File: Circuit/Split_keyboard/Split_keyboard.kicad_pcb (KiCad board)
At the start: 2 copper layers, 62 parts, among them SW27 SW_Push, SW28 SW_Push, SW29 SW_Push, SW30 SW_Push, SW31 SW_Push, SW32 SW_Push, SW33 SW_Push, SW34 SW_Push, SW35 SW_Push, SW36 SW_Push, SW37 SW_Push, SW38 SW_Push, SW39 SW_Push, SW40 SW_Push, SW41 SW_Push, SW42 SW_Push, SW43 SW_Push, SW44 SW_Push, SW45 SW_Push, SW46 SW_Push, SW47 SW_Push, SW48 SW_Push, SW49 SW_Push, SW50 SW_Push, SW51 SW_Push, SW52 SW_Push, U2 XIAO-nRF52840-SMD

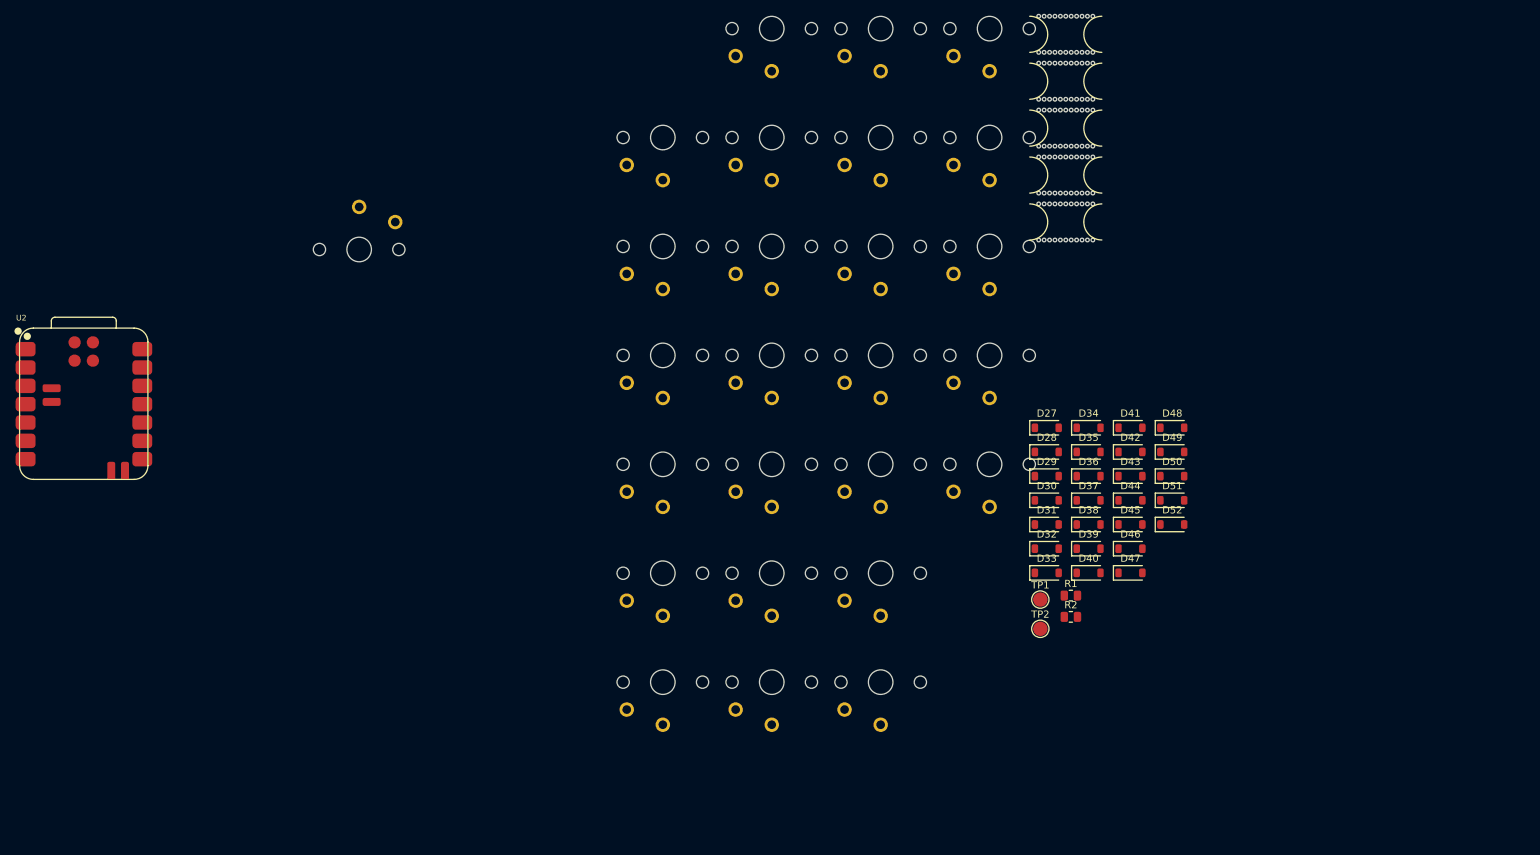
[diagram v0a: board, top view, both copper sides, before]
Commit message: Changed the design of the footprints and maded it simliar to keeb.io keyboards
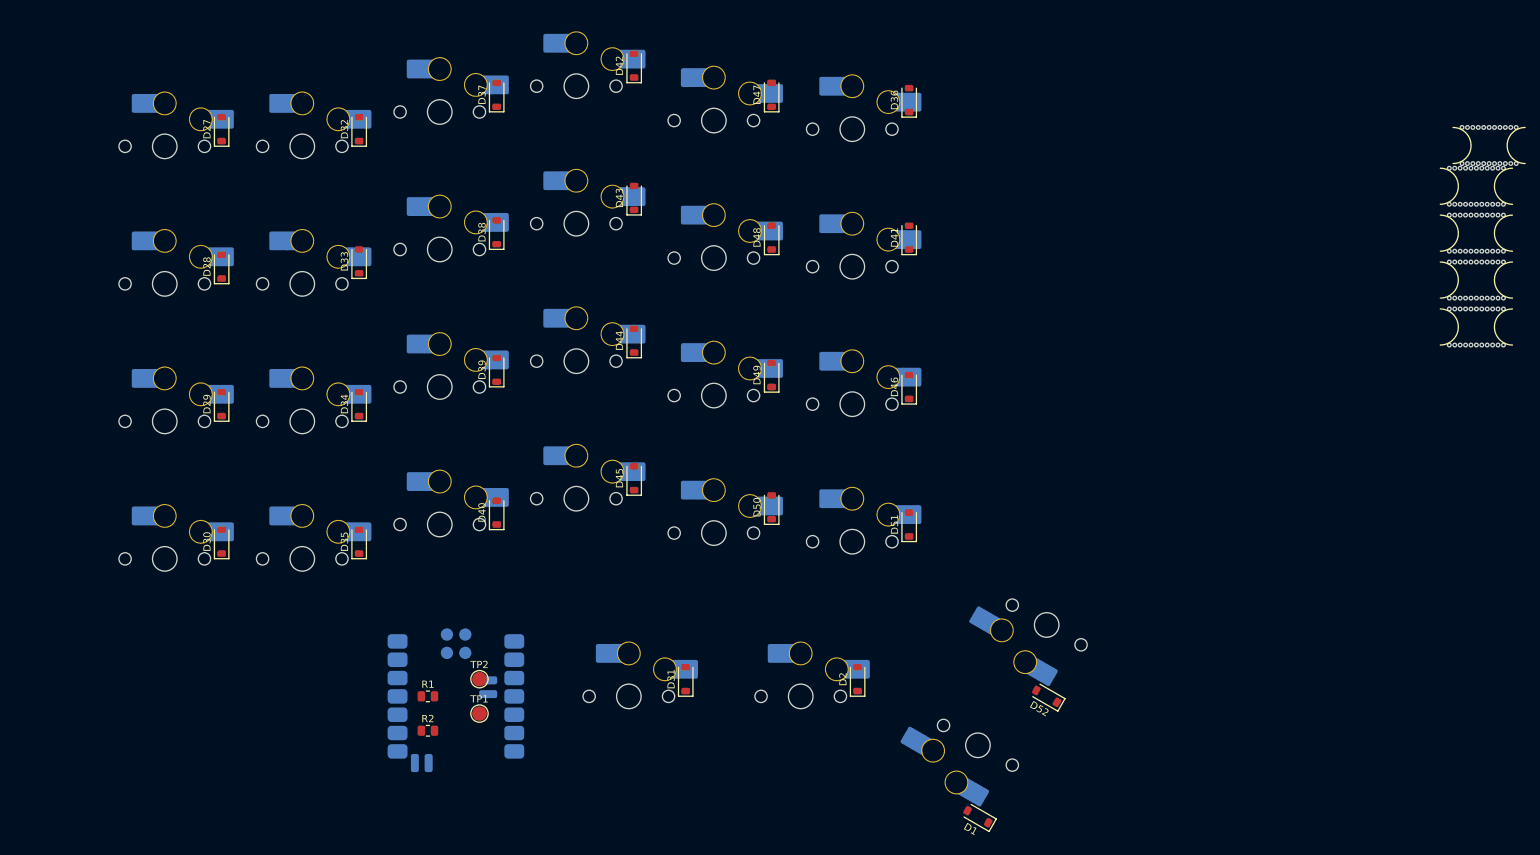
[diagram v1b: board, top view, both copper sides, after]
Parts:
- added D1: D, Diode_SMD:D_SOD-123, F.Cu at (169.1, 157.2)
- added D2: D, Diode_SMD:D_SOD-123, F.Cu at (152.4, 138.1)
- added SW1: SW_Push, marbastlib-choc:SW_choc_v1_HS_CPG135001S30_1u, B.Cu at (169.1, 147.3)
- added SW2: SW_Push, marbastlib-choc:SW_choc_v1_HS_CPG135001S30_1u, B.Cu at (144.5, 140.5)
- SW27, SW28, SW29, SW30, SW31, SW32, SW33, SW34, SW35, SW36, SW37, SW38, SW39, SW40, SW41, SW42, SW43, SW44, SW45, SW46, SW47, SW48, SW49, SW50, SW51, SW52: footprint marbastlib-choc:SW_choc_v1_1u -> marbastlib-choc:SW_choc_v1_HS_CPG135001S30_1u; moved to B.Cu
- U2: moved to B.Cu
- moved D27 121.6 mm to (64.3, 61.9), turned to 90 degrees
- moved D28 117.2 mm to (64.3, 81.0), turned to 90 degrees
- moved D29 114.7 mm to (64.3, 100.0), turned to 90 degrees
- moved D30 114.5 mm to (64.3, 119.1), turned to 90 degrees
- moved D32 111.6 mm to (83.3, 61.9), turned to 90 degrees
- moved D33 104.6 mm to (83.3, 80.2), turned to 90 degrees
- moved D35 101.8 mm to (83.3, 119.1), turned to 90 degrees
- moved D34 101.1 mm to (83.3, 100.0), turned to 90 degrees
- moved D37 99.4 mm to (102.4, 57.1), turned to 90 degrees
- moved D38 91.5 mm to (102.4, 76.2), turned to 90 degrees
- moved R2 90.5 mm to (92.9, 145.3)
- moved R1 90.2 mm to (92.9, 140.5)
- moved SW35 87.4 mm to (75.5, 121.4)
- moved D42 87.1 mm to (121.4, 53.1), turned to 90 degrees
- moved D39 85.7 mm to (102.4, 95.2), turned to 90 degrees
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
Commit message: Added right side and added edge.cuts for the pcb on both sides
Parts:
- added BO10: Break Off, Panelization.pretty-master:mouse-bite-5mm-slot, F.Cu at (175.5, 67.5)
- added BO6: Break Off, Panelization.pretty-master:mouse-bite-5mm-slot, F.Cu at (172.9, 38.6)
- added BO7: Break Off, Panelization.pretty-master:mouse-bite-5mm-slot, F.Cu at (172.9, 45.1)
- added BO8: Break off, Panelization.pretty-master:mouse-bite-5mm-slot, F.Cu at (172.9, 51.6)
- added BO9: Break Off, Panelization.pretty-master:mouse-bite-5mm-slot, F.Cu at (172.9, 58.1)
- added D10: D, Diode_SMD:D_SOD-123, B.Cu at (192.9, 81.0)
- added D11: D, Diode_SMD:D_SOD-123, B.Cu at (288.1, 61.9)
- added D12: D, Diode_SMD:D_SOD-123, B.Cu at (269.1, 81.0)
- added D13: D, Diode_SMD:D_SOD-123, B.Cu at (250.0, 115.0)
- added D14: D, Diode_SMD:D_SOD-123, B.Cu at (250.0, 60.3)
- added D15: D, Diode_SMD:D_SOD-123, B.Cu at (231.0, 57.1)
- added D16: D, Diode_SMD:D_SOD-123, B.Cu at (231.0, 76.2)
- added D17: D, Diode_SMD:D_SOD-123, B.Cu at (192.9, 61.9)
- added D18: D, Diode_SMD:D_SOD-123, B.Cu at (288.1, 81.0)
- added D19: D, Diode_SMD:D_SOD-123, B.Cu at (269.1, 98.4)
- added D20: D, Diode_SMD:D_SOD-123, B.Cu at (269.1, 61.9)
- added D21: D, Diode_SMD:D_SOD-123, B.Cu at (250.0, 96.0)
- added D22: D, Diode_SMD:D_SOD-123, B.Cu at (250.0, 78.6)
- added D23: D, Diode_SMD:D_SOD-123, B.Cu at (192.9, 98.4)
- added D24: D, Diode_SMD:D_SOD-123, B.Cu at (288.1, 119.1)
- added D25: D, Diode_SMD:D_SOD-123, B.Cu at (288.1, 98.4)
- added D26: D, Diode_SMD:D_SOD-123, B.Cu at (269.1, 117.4)
- added D3: D, Diode_SMD:D_SOD-123, B.Cu at (192.9, 119.1)
- added D4: D, Diode_SMD:D_SOD-123, B.Cu at (211.9, 115.0)
- added D5: D, Diode_SMD:D_SOD-123, B.Cu at (211.9, 96.0)
- added D53: D, Diode_SMD:D_SOD-123, B.Cu at (226.2, 140.5)
- added D54: D, Diode_SMD:D_SOD-123, B.Cu at (192.9, 150.0)
- added D55: D, Diode_SMD:D_SOD-123, B.Cu at (202.4, 140.5)
- added D56: D, Diode_SMD:D_SOD-123, B.Cu at (181.0, 135.7)
- added D6: D, Diode_SMD:D_SOD-123, B.Cu at (231.0, 114.3)
- added D7: D, Diode_SMD:D_SOD-123, B.Cu at (231.0, 95.2)
- added D8: D, Diode_SMD:D_SOD-123, B.Cu at (211.9, 59.5)
- added D9: D, Diode_SMD:D_SOD-123, B.Cu at (211.9, 78.6)
- added R3: 806k, Resistor_SMD:R_0805_2012Metric, F.Cu at (278.7, 27.9)
- added R4: 2M, Resistor_SMD:R_0805_2012Metric, F.Cu at (278.7, 30.8)
- added SW10: SW_Push, marbastlib-choc:SW_choc_v1_HS_CPG135001S30_1u, B.Cu at (200.8, 81.0)
- added SW11: SW_Push, marbastlib-choc:SW_choc_v1_HS_CPG135001S30_1u, B.Cu at (296.0, 61.9)
- added SW12: SW_Push, marbastlib-choc:SW_choc_v1_HS_CPG135001S30_1u, B.Cu at (277.0, 81.0)
- added SW13: SW_Push, marbastlib-choc:SW_choc_v1_HS_CPG135001S30_1u, B.Cu at (257.9, 116.7)
- added SW14: SW_Push, marbastlib-choc:SW_choc_v1_HS_CPG135001S30_1u, B.Cu at (257.9, 59.5)
- added SW15: SW_Push, marbastlib-choc:SW_choc_v1_HS_CPG135001S30_1u, B.Cu at (238.9, 57.1)
- added SW16: SW_Push, marbastlib-choc:SW_choc_v1_HS_CPG135001S30_1u, B.Cu at (238.9, 76.2)
- added SW17: SW_Push, marbastlib-choc:SW_choc_v1_HS_CPG135001S30_1u, B.Cu at (200.8, 61.9)
- added SW18: SW_Push, marbastlib-choc:SW_choc_v1_HS_CPG135001S30_1u, B.Cu at (296.0, 81.0)
- added SW19: SW_Push, marbastlib-choc:SW_choc_v1_HS_CPG135001S30_1u, B.Cu at (277.0, 100.0)
- added SW20: SW_Push, marbastlib-choc:SW_choc_v1_HS_CPG135001S30_1u, B.Cu at (277.0, 61.9)
- added SW21: SW_Push, marbastlib-choc:SW_choc_v1_HS_CPG135001S30_1u, B.Cu at (257.9, 97.6)
- added SW22: SW_Push, marbastlib-choc:SW_choc_v1_HS_CPG135001S30_1u, B.Cu at (257.9, 78.6)
- added SW23: SW_Push, marbastlib-choc:SW_choc_v1_HS_CPG135001S30_1u, B.Cu at (200.8, 100.0)
- added SW24: SW_Push, marbastlib-choc:SW_choc_v1_HS_CPG135001S30_1u, B.Cu at (296.0, 119.1)
- added SW25: SW_Push, marbastlib-choc:SW_choc_v1_HS_CPG135001S30_1u, B.Cu at (296.0, 100.0)
- added SW26: SW_Push, marbastlib-choc:SW_choc_v1_HS_CPG135001S30_1u, B.Cu at (277.0, 119.1)
- added SW3: SW_Push, marbastlib-choc:SW_choc_v1_HS_CPG135001S30_1u, B.Cu at (200.8, 119.1)
- added SW4: SW_Push, marbastlib-choc:SW_choc_v1_HS_CPG135001S30_1u, B.Cu at (219.8, 116.7)
- added SW5: SW_Push, marbastlib-choc:SW_choc_v1_HS_CPG135001S30_1u, B.Cu at (219.8, 97.6)
- added SW53: SW_Push, marbastlib-choc:SW_choc_v1_HS_CPG135001S30_1u, B.Cu at (234.1, 140.5)
- added SW54: SW_Push, marbastlib-choc:SW_choc_v1_HS_CPG135001S30_1u, B.Cu at (185.7, 144.9)
- added SW55: SW_Push, marbastlib-choc:SW_choc_v1_HS_CPG135001S30_1u, B.Cu at (210.3, 140.5)
- added SW56: SW_Push, marbastlib-choc:SW_choc_v1_HS_CPG135001S30_1u, B.Cu at (176.2, 128.6)
- added SW6: SW_Push, marbastlib-choc:SW_choc_v1_HS_CPG135001S30_1u, B.Cu at (238.9, 114.3)
- added SW7: SW_Push, marbastlib-choc:SW_choc_v1_HS_CPG135001S30_1u, B.Cu at (238.9, 95.2)
- added SW8: SW_Push, marbastlib-choc:SW_choc_v1_HS_CPG135001S30_1u, B.Cu at (219.8, 59.5)
- added SW9: SW_Push, marbastlib-choc:SW_choc_v1_HS_CPG135001S30_1u, B.Cu at (219.8, 78.6)
- added TP3: BAT, TestPoint:TestPoint_Pad_D2.0mm, F.Cu at (269.9, 36.1)
- added TP4: TestPoint, TestPoint:TestPoint_Pad_D2.0mm, F.Cu at (274.7, 19.4)
- added U1: XIAO-nRF52840-SMD, OPL_Kicad:XIAO-nRF52840-SMD, B.Cu at (257.2, 138.1)
- D1, D2, D27, D28, D29, D30, D31, D32, D33, D34, D35, D36, D37, D38, D39, D40, D41, D42, D43, D44, D45, D46, D47, D48, D49, D50, D51, D52: moved to B.Cu
- moved BO2 95.2 mm to (146.1, 45.1)
- moved BO3 95.2 mm to (146.1, 51.6)
- moved BO4 95.2 mm to (146.1, 58.1)
- moved BO1 95.2 mm to (147.9, 39.5)
- moved BO5 91.2 mm to (150.1, 65.6)
- moved D2 56.8 mm to (95.7, 142.2)
- moved D33 33.5 mm to (50.5, 86.7)
- moved D42 33.3 mm to (88.6, 58.9)
- moved D43 33.3 mm to (88.6, 77.2)
- moved D44 33.3 mm to (88.6, 97.0)
- moved D45 33.3 mm to (88.6, 116.0)
- moved D47 33.2 mm to (107.7, 62.2)
- moved D48 33.2 mm to (107.7, 82.0)
- moved D49 33.2 mm to (107.7, 101.0)
- moved D50 33.2 mm to (107.7, 119.3)
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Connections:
- D1 pad 1: R6 -> R1
- D2 pad 1: R6 -> R2
- D27 pad 1: R1 -> R5
- D28 pad 1: R2 -> R6
- D29 pad 1: R3 -> R1
- D30 pad 1: R4 -> R2
- D31 pad 1: R5 -> R3
- D32 pad 1: R1 -> R4
- D33 pad 1: R2 -> R5
- D34 pad 1: R3 -> R1
- D35 pad 1: R4 -> R2
- D36 pad 1: R5 -> R3
- D37 pad 1: R1 -> R4
- D38 pad 1: R2 -> R5
- D39 pad 1: R3 -> R1
- D40 pad 1: R4 -> R2
- D41 pad 1: R5 -> R3
- D42 pad 1: R1 -> R4
- D43 pad 1: R2 -> R5
- D44 pad 1: R3 -> R6
- D45 pad 1: R4 -> R1
- D46 pad 1: R5 -> R2
- D47 pad 1: R1 -> R3
- D48 pad 1: R2 -> R4
- D49 pad 1: R3 -> R5
- D50 pad 1: R4 -> R6
- D51 pad 1: R5 -> R1
- D52 pad 1: R6 -> R2
- SW1 pad 1: C4 -> C1
- SW2 pad 1: C3 -> C1
- SW27 pad 1: C1 -> C5
- SW28 pad 1: C1 -> C5
- SW32 pad 1: C2 -> C1
- SW33 pad 1: C2 -> C1
- SW37 pad 1: C3 -> C2
- SW38 pad 1: C3 -> C2
- SW42 pad 1: C4 -> C3
- SW43 pad 1: C4 -> C3
- SW44 pad 1: C4 -> C3
- SW47 pad 1: C5 -> C4
- SW48 pad 1: C5 -> C4
- SW49 pad 1: C5 -> C4
- SW50 pad 1: C5 -> C4
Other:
- board outline added: 294.8 x 119.5 mm

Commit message: Changed the design of the keyboard completelty with schematis
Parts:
- removed BO1, BO10, BO2, BO4, BO5, BO9: Break Off, Panelization.pretty-master:mouse-bite-5mm-slot
- removed BO3: Break off, Panelization.pretty-master:mouse-bite-5mm-slot
- removed U1, U2: XIAO-nRF52840-SMD, OPL_Kicad:XIAO-nRF52840-SMD
- added U3: SuperMini nRF52840, PCM_marbastlib-xp-promicroish:SuperMini_nRF52840_AH_USBup, F.Cu at (304.8, 144.8)
- added U4: SuperMini nRF52840, PCM_marbastlib-xp-promicroish:SuperMini_nRF52840_AH_USBup, F.Cu at (27.9, 144.8)
- R1, R2, R3, R4: moved to B.Cu
- moved SW28 289.0 mm to (309.9, 121.9)
- moved SW27 288.9 mm to (309.9, 101.6)
- moved D28 272.7 mm to (302.3, 116.8)
- moved D27 272.5 mm to (302.3, 96.5)
- moved R3 255.2 mm to (54.2, 149.1)
- moved R4 252.6 mm to (53.3, 144.8)
- moved TP4 251.7 mm to (61.0, 152.4), turned to 180 degrees
- moved TP3 233.3 mm to (63.5, 144.8), turned to 180 degrees
- moved D53 229.7 mm to (12.7, 55.9), turned to 90 degrees
- moved SW53 228.1 mm to (20.3, 61.0)
- moved R1 211.5 mm to (271.5, 134.6)
- moved TP2 207.8 mm to (275.0, 137.2), turned to 180 degrees
- moved R2 206.9 mm to (266.7, 134.6)
- moved TP1 205.4 mm to (272.6, 144.3), turned to 180 degrees
- moved D55 194.7 mm to (12.7, 96.5), turned to 90 degrees
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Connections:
- D10 pad 1: R5 -> R4
- D11 pad 1: R1 -> R5
- D12 pad 1: R2 -> R1
- D13 pad 1: R3 -> R2
- D14 pad 1: R4 -> R3
- D15 pad 1: R5 -> R4
- D16 pad 1: R6 -> R5
- D21 pad 1: R5 -> R1
- D22 pad 1: R6 -> R2
- D23 pad 1: R1 -> R3
- D24 pad 1: R2 -> R4
- D25 pad 1: R3 -> R1
- D26 pad 1: R4 -> R2
- D27 pad 1: R5 -> R3
- D28 pad 1: R6 -> R4
- D34 pad 1: R1 -> R6
- D35 pad 1: R2 -> R1
- D36 pad 1: R3 -> R2
- D37 pad 1: R4 -> R3
- D38 pad 1: R5 -> R4
- D39 pad 1: R1 -> R5
- D40 pad 1: R2 -> R1
- D41 pad 1: R3 -> R2
- D42 pad 1: R4 -> R3
- D43 pad 1: R5 -> R4
- D44 pad 1: R6 -> R5
- D49 pad 1: R5 -> R1
- D50 pad 1: R6 -> R2
- D51 pad 1: R1 -> R3
- D52 pad 1: R2 -> R4
- D53 pad 1: R3 -> R1
- D54 pad 1: R4 -> R2
- D55 pad 1: R5 -> R3
- D56 pad 1: R6 -> R4
- D6 pad 1: R1 -> R6
- D7 pad 1: R2 -> R1
- D8 pad 1: R3 -> R2
- D9 pad 1: R4 -> R3
- SW11 pad 1: C3 -> C2
- SW21 pad 1: C4 -> C5
- SW22 pad 1: C4 -> C5
- SW25 pad 1: C5 -> C6
- SW26 pad 1: C5 -> C6
- SW27 pad 1: C5 -> C6
- SW28 pad 1: C5 -> C6
- SW34 pad 1: C2 -> C1
- SW39 pad 1: C3 -> C2
- SW49 pad 1: C4 -> C5
- SW50 pad 1: C4 -> C5
- SW53 pad 1: C5 -> C6
- SW54 pad 1: C5 -> C6
- SW55 pad 1: C5 -> C6
- SW56 pad 1: C5 -> C6
- SW6 pad 1: C2 -> C1
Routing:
- net R2: track 0.00 -> 525.6 mm
- net R1: track 0.00 -> 423.5 mm
- net R3: track 0.00 -> 409.0 mm
- net R4: track 0.00 -> 295.1 mm
- net R5: track 0.00 -> 259.4 mm
- net R6: track 0.00 -> 250.3 mm
- net C1: track 0.00 -> 230.9 mm
- net C2: track 0.00 -> 191.3 mm
- net C3: track 0.00 -> 185.7 mm
- net C5: track 0.00 -> 130.8 mm
- net C4: track 0.00 -> 130.1 mm
- net C6: track 0.00 -> 130.1 mm
- net GND: track 0.00 -> 41.2 mm
- net BT_PIN: track 0.00 -> 38.7 mm
- net Net-(D23-A): track 0.00 -> 14.3 mm
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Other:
- board size 294.8 x 119.5 mm -> 312.9 x 117 mm
